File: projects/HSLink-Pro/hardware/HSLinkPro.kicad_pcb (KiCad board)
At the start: 4 copper layers, 26 x 35 mm, 126 parts, among them J1 IDC 2x10p 夹板, J2 USB_C_Receptacle_USB2.0, J3 Header 1.27 4P, Q1 AO3401A, Q2 2N7002, Q3 AO3401A, Q4 2N7002, SW1 1TS028A-1900-0600-CT, U1 HPM5301IEG1, U10 EA3036C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

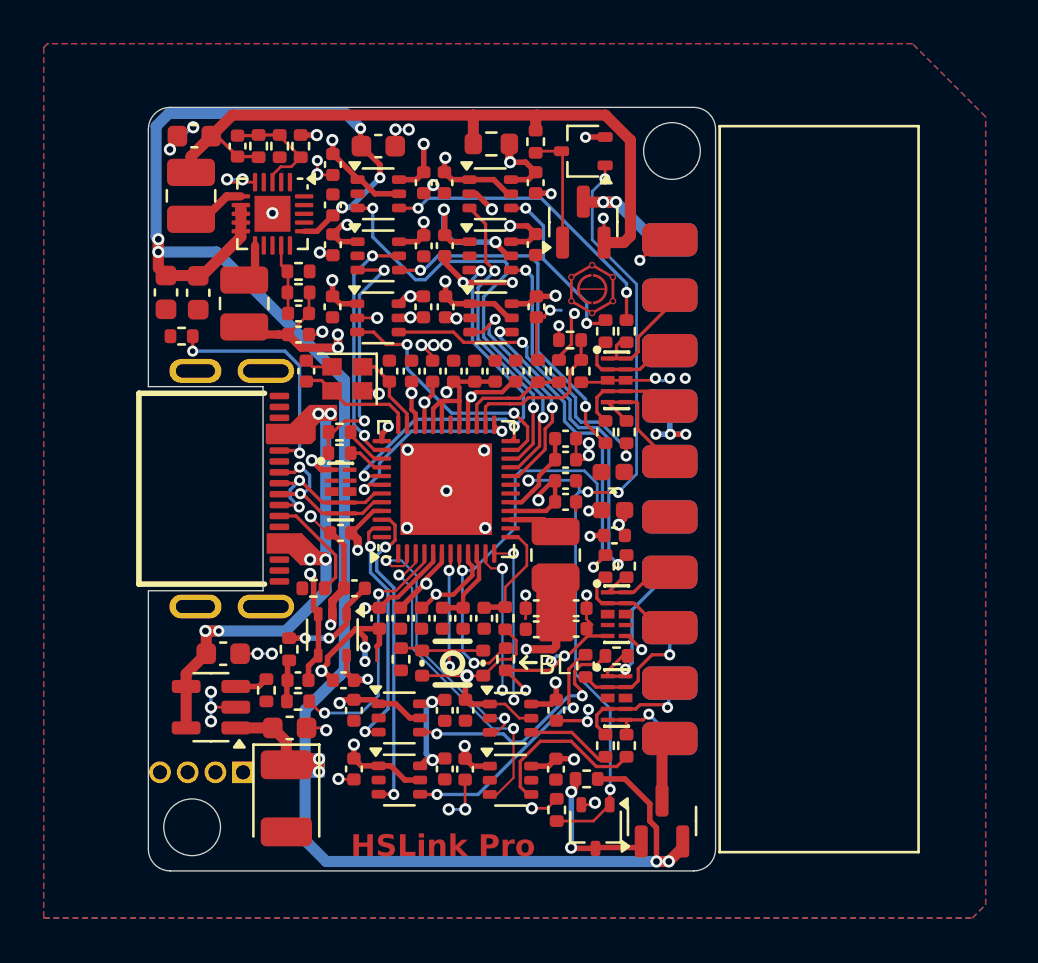
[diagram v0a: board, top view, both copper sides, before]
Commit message: HSLink-Pro: 2.3.1 (#29)
* update: 更新电源部分

* update: 更新原理图

* update: 更新PCB

- 修改定位孔位置
- 修改Type-C位置

* update: 添加RTT LOGO

* chore: 添加cJSON库

* feat: 添加与上位机的HID通信接口

* refactor: 重构命令解析部分代码

* fix: 修复描述符错误

* feat: 添加上位机下发设置功能

* feat: 添加数据保存

* fix: 修复可能的一些错误

* fix: 修复写入flash死机问题

* fix: 潜在的内存泄露问题

* chore: 添加tlsf

* chore: 切换cJSON库位置

* feat: 内存管理切换为tlsf

* feat: 添加首次默认设置

* feat: 添加硬件版本号

* feat: 添加获取设置

* chore: 将项目修改为cpp

* feat: 重构为cpp

* fix: 修复release下可能会崩溃的玄学问题

* chore: 删除cJSON库

* fix: 修复RapidJSON库所需内存

* fix: 修复nickname设置问题

* fix: BL工程编译失败

* fix: BL工程里面关闭所有输出

* fix: 修复一些warning

* update: README

* fix: get_setting字段错误

* update: 1.2.0硬件

* style: 统一接口命名

* feat: 添加upgrade命令

* fix: 将硬件版本号放在OTP寄存器中

* fix: 解决初始值问题

* fix: PWM输出极性反了

* fix: 1.2.0硬件修改IO

* release: 2.3.1
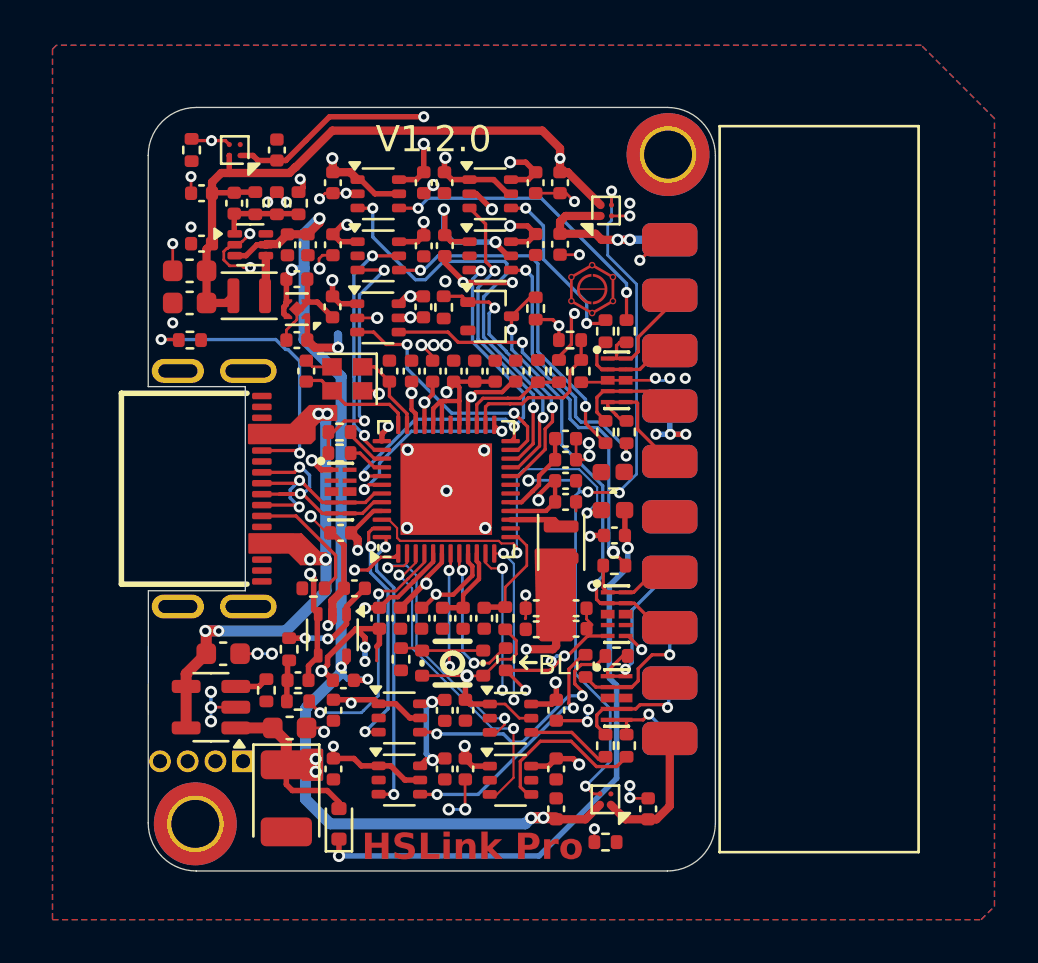
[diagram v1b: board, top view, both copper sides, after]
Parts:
- removed C35: 0.1u, Capacitor_SMD:C_0402_1005Metric
- removed L3: 1.5u, Inductor_SMD:L_1008_2520Metric
- removed Q2, Q4: 2N7002, Package_TO_SOT_SMD:SOT-323_SC-70
- removed Q3: AO3401A, Package_TO_SOT_SMD:SOT-23
- removed R19, R20: 100k, Resistor_SMD:R_0402_1005Metric
- removed R29: 100R, Resistor_SMD:R_0402_1005Metric
- removed U7: SN74LVC1T45DCK, Package_TO_SOT_SMD:SOT-363_SC-70-6
- added C59: 1u, Capacitor_SMD:C_0402_1005Metric, F.Cu at (115.7, 59.2)
- added C60: 1u, Capacitor_SMD:C_0402_1005Metric, F.Cu at (111.7, 30.5)
- added C61: 1u, Capacitor_SMD:C_0402_1005Metric, F.Cu at (111.7, 33.3)
- added C62: 1u, Capacitor_SMD:C_0402_1005Metric, F.Cu at (95.3, 31.0)
- added C63: 1u, Capacitor_SMD:C_0402_1005Metric, F.Cu at (98.7, 29.0)
- added D2: 1N5819, Diode_SMD:D_SOD-523, F.Cu at (101.6, 59.9)
- added G***: LOGO, LOGO, B.Cu at (105.9, 29.5)
- added REF**: MountingHole_2.2mm_M2_DIN965_Pad_TopBottom, MountingHole:MountingHole_2.2mm_M2_DIN965_Pad_TopBottom, F.Cu at (116.7, 29.2)
- added REF**: MountingHole_2.2mm_M2_DIN965_Pad_TopBottom, MountingHole:MountingHole_2.2mm_M2_DIN965_Pad_TopBottom, F.Cu at (95.0, 59.9)
- added U19: ME6211C33U4G, Package_DFN_QFN:OnSemi_XDFN4-1EP_1.0x1.0mm_EP0.52x0.52mm, F.Cu at (99.6, 36.3)
- added U20: AW3512, Package_CSP:WLCSP-4-X1-WLB0909-4_0.89x0.89mm_P0.5mm, F.Cu at (113.8, 58.7)
- added U21: AW3512, Package_CSP:WLCSP-4-X1-WLB0909-4_0.89x0.89mm_P0.5mm, F.Cu at (113.8, 31.8)
- added U22: AW3512, Package_CSP:WLCSP-4-X1-WLB0909-4_0.89x0.89mm_P0.5mm, F.Cu at (96.8, 29.0)
- C40: value 1u -> 4.7u
- C41, C46: value 10u -> 22u
- C47: value 10u -> 0.1u; footprint Capacitor_SMD:C_0603_1608Metric -> Capacitor_SMD:C_0402_1005Metric
- C48: value 10u -> 1u
- C49: value 220p -> 1u
- C50: value 220p -> 6.8p
- C51: value 10u -> 1u; footprint Capacitor_SMD:C_0603_1608Metric -> Capacitor_SMD:C_0402_1005Metric
- L1: footprint Inductor_SMD:L_1008_2520Metric -> Inductor_SMD:L_Murata_DFE201610P
- L2: value 1.5u -> 2.2uH; footprint Inductor_SMD:L_1008_2520Metric -> Inductor_SMD:L_Murata_DFE201610P
- Q1: value AO3401A -> 2N7002; footprint Package_TO_SOT_SMD:SOT-23 -> Package_TO_SOT_SMD:SOT-323_SC-70
- R13: value 0R -> 1k; footprint Resistor_SMD:R_0603_1608Metric -> Resistor_SMD:R_0402_1005Metric
- R2: value 22.1k -> 100k
- U10: value EA3036C -> TLV62568DRL; footprint Package_DFN_QFN:QFN-20-1EP_3x3mm_P0.4mm_EP1.65x1.65mm -> Package_TO_SOT_SMD:SOT-563
- moved C51 35.0 mm to (111.5, 59.2), turned to 90 degrees
- moved C34 25.4 mm to (99.2, 33.3), turned to -90 degrees
- moved Q1 24.4 mm to (108.5, 36.6), turned to 0 degrees
- moved C53 21.8 mm to (101.8, 53.3), turned to 180 degrees
- moved C45 21.2 mm to (111.5, 57.4)
- moved C44 21.2 mm to (107.4, 57.4)
- moved C40 20.0 mm to (100.2, 33.3), turned to -90 degrees
- moved C47 9.25 mm to (95.3, 33.3), turned to 180 degrees
- moved R13 7.81 mm to (110.6, 36.2), turned to 90 degrees
- moved R2 7.41 mm to (94.8, 29.0), turned to -90 degrees
- moved R3 6.69 mm to (106.4, 36.2), turned to -90 degrees
- moved R21 2.68 mm to (113.8, 60.7), turned to 0 degrees
- moved C50 2.62 mm to (96.8, 31.4), turned to -90 degrees
- moved R4 2.62 mm to (97.7, 31.4), turned to -90 degrees
- moved R6 2.62 mm to (98.7, 31.4), turned to 90 degrees
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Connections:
- C34 pad 1: GND -> +5V
- C34 pad 2: +3V3 -> GND
- C41 pad 1: +5V -> TRANS_VCC
- C46 pad 1: +5V -> TRANS_VCC
- C47 pad 1: +5V -> TRANS_VCC
- C48 pad 1: GND -> +5V
- C48 pad 2: +3V3 -> GND
- C49 pad 1: Net-(U10A-FB1) -> +3V3
- C49 pad 2: +3V3 -> GND
- C51 pad 1: TRANS_VCC -> +5V
- C57 pad 1: +3V3 -> Net-(D1-VDD)
- D1 pad 1: +3V3 -> Net-(D1-VDD)
- D1 pad 4: /BOOT0 -> /WS2812
- L2 pad 1: +3V3 -> Net-(U10-SW)
- L2 pad 2: Net-(U10A-LX1) -> TRANS_VCC
- Q1 pad 1: Net-(Q1-G) -> /SRST
- Q1 pad 2: +5V -> GND
- Q1 pad 3: +5V_OUT -> /Interface /SRST
- R13 pad 2: VEE -> /Interface /SRST
- R2 pad 1: Net-(U10A-FB1) -> /PORT_EN
- R3 pad 1: Net-(U10A-FB1) -> /SRST
- R3 pad 2: +3V3 -> GND
- U1 pad 1: unconnected-(U1B-PA04/URT1.CTS/SPI0.CS0/TRGM0.P04/JTAG.TDO-Pad1) -> /PORT_EN
- U1 pad 46: /UART_RTS -> /WS2812
- U1 pad 48: unconnected-(U1B-PA05/TMR1.COMP2/URT1.DE/URT1.RTS/SPI0.SCLK/TRGM0.P05/JTAG.TDI-Pad48) -> /UART_RTS
- U10 pad 1: GND -> /Power/TRANS_FB
- U10 pad 2: unconnected-(U10C-FB3-Pad2) -> GND
- U10 pad 3: /Power/TRANS_FB -> +5V
- U10 pad 4: GND -> Net-(U10-SW)
- U10 pad 5: GND -> +5V
- U10 pad 6: Net-(U10B-LX2) -> unconnected-(U10-NC-Pad6)
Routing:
- net +5V: track 96.5 -> 61.0 mm, vias 10 -> 8
- net /PORT_EN: track 0.00 -> 28.7 mm, vias 0 -> 2
- net Net-(D1-VDD): track 0.00 -> 27.8 mm, vias 0 -> 2
- net /WS2812: track 0.00 -> 16.9 mm, vias 0 -> 2
- net /Interface /SRST: track 4.43 -> 19.8 mm, vias 0 -> 2
- net Net-(U7-B): track 14.7 -> 0.00 mm, vias 2 -> 0
- net +3V3: track 154.4 -> 140.3 mm, vias 18 -> 16
- net /BOOT0: track 18.6 -> 6.97 mm, vias 3 -> 2
- net VEE: track 77.8 -> 86.2 mm
- net Net-(Q1-G): track 6.42 -> 0.00 mm, vias 2 -> 0
- net Net-(Q3-G): track 5.25 -> 0.00 mm
- net TRANS_VCC_OUT: track 4.51 -> 8.23 mm
- net +5V_OUT: track 2.77 -> 6.33 mm
- net Net-(U10A-FB1): track 3.21 -> 0.00 mm
- net Net-(J2-CC1): track 10.8 -> 13.4 mm
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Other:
- outline, holes or cut-outs redrawn
- copper layers 4 -> 6
- board text added: "V1.2.0"
